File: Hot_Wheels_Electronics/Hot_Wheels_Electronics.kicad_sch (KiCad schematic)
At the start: 21 parts, among them J1 motor_output_a, J2 motor_output_b, J3 Conn_01x05_Socket, M1 motor_driver: DRV8833PW, SW1 main_switch, U1 esp32-wemos-d1-mini, U2 ESP32-WROOM-32, U3 BMI160, U4 QITN BEC

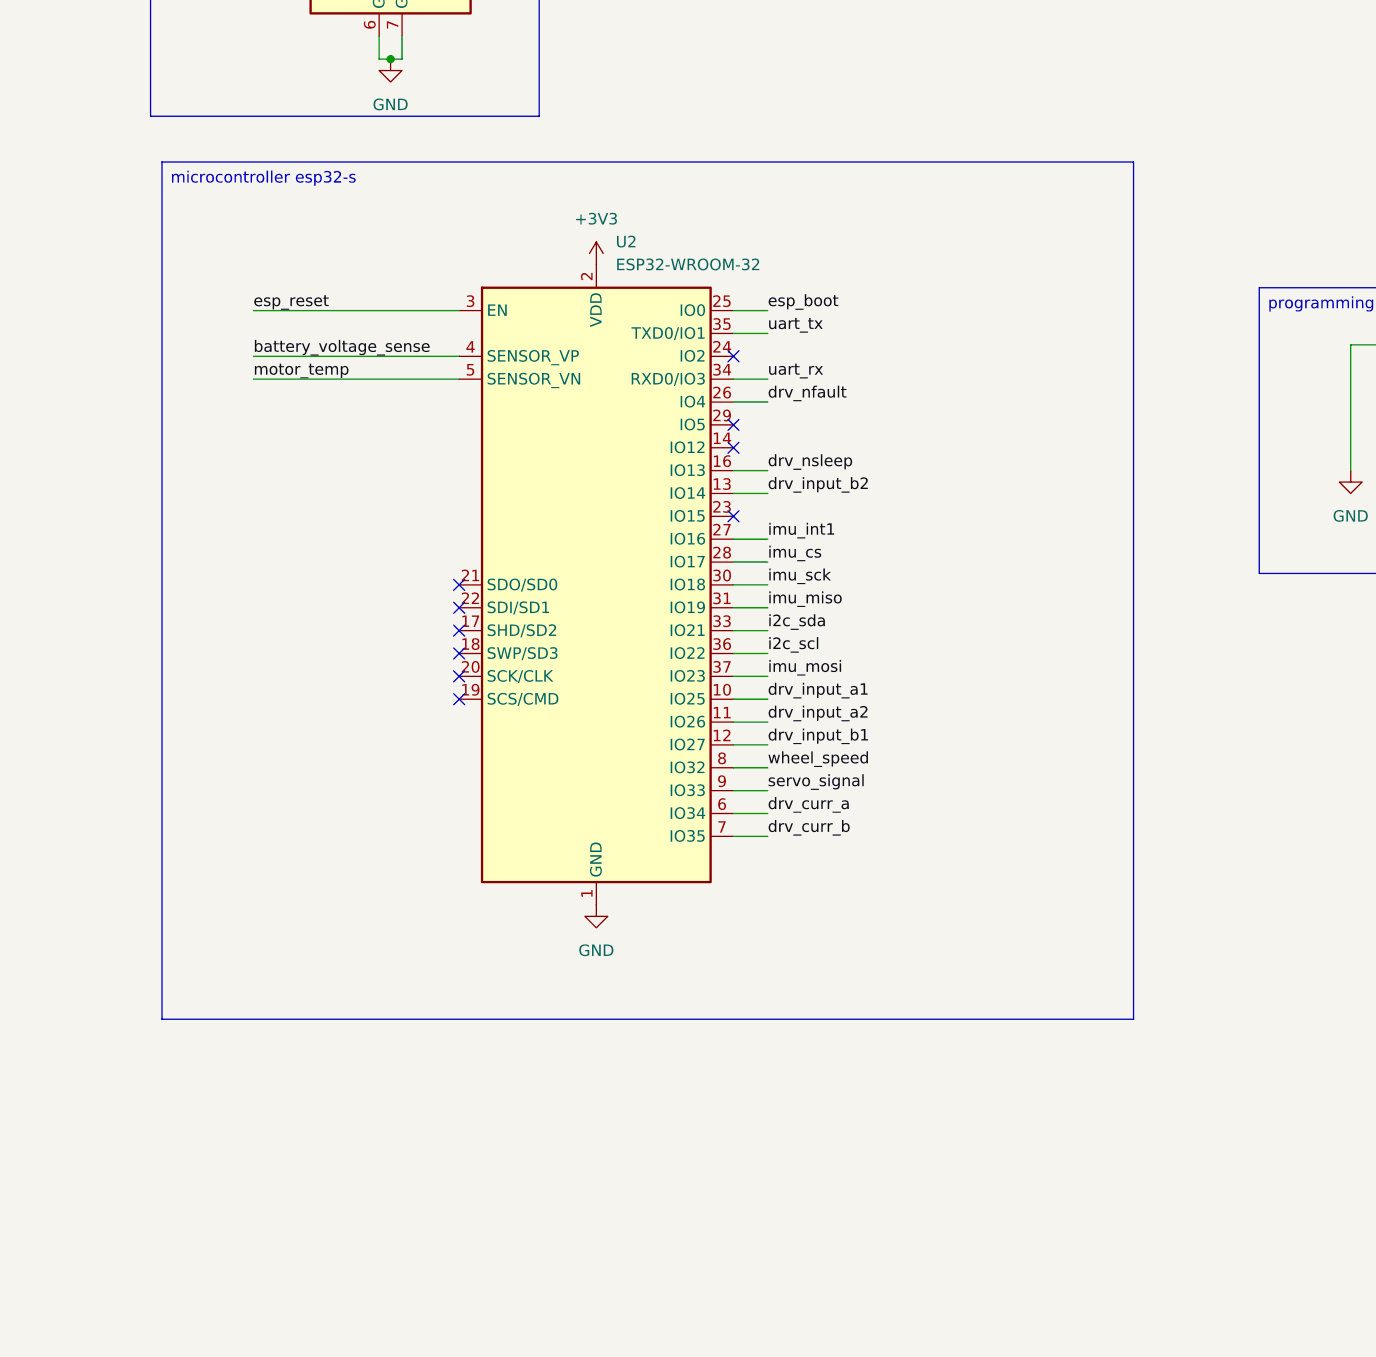
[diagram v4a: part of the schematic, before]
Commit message: add the reset and boot schematic components
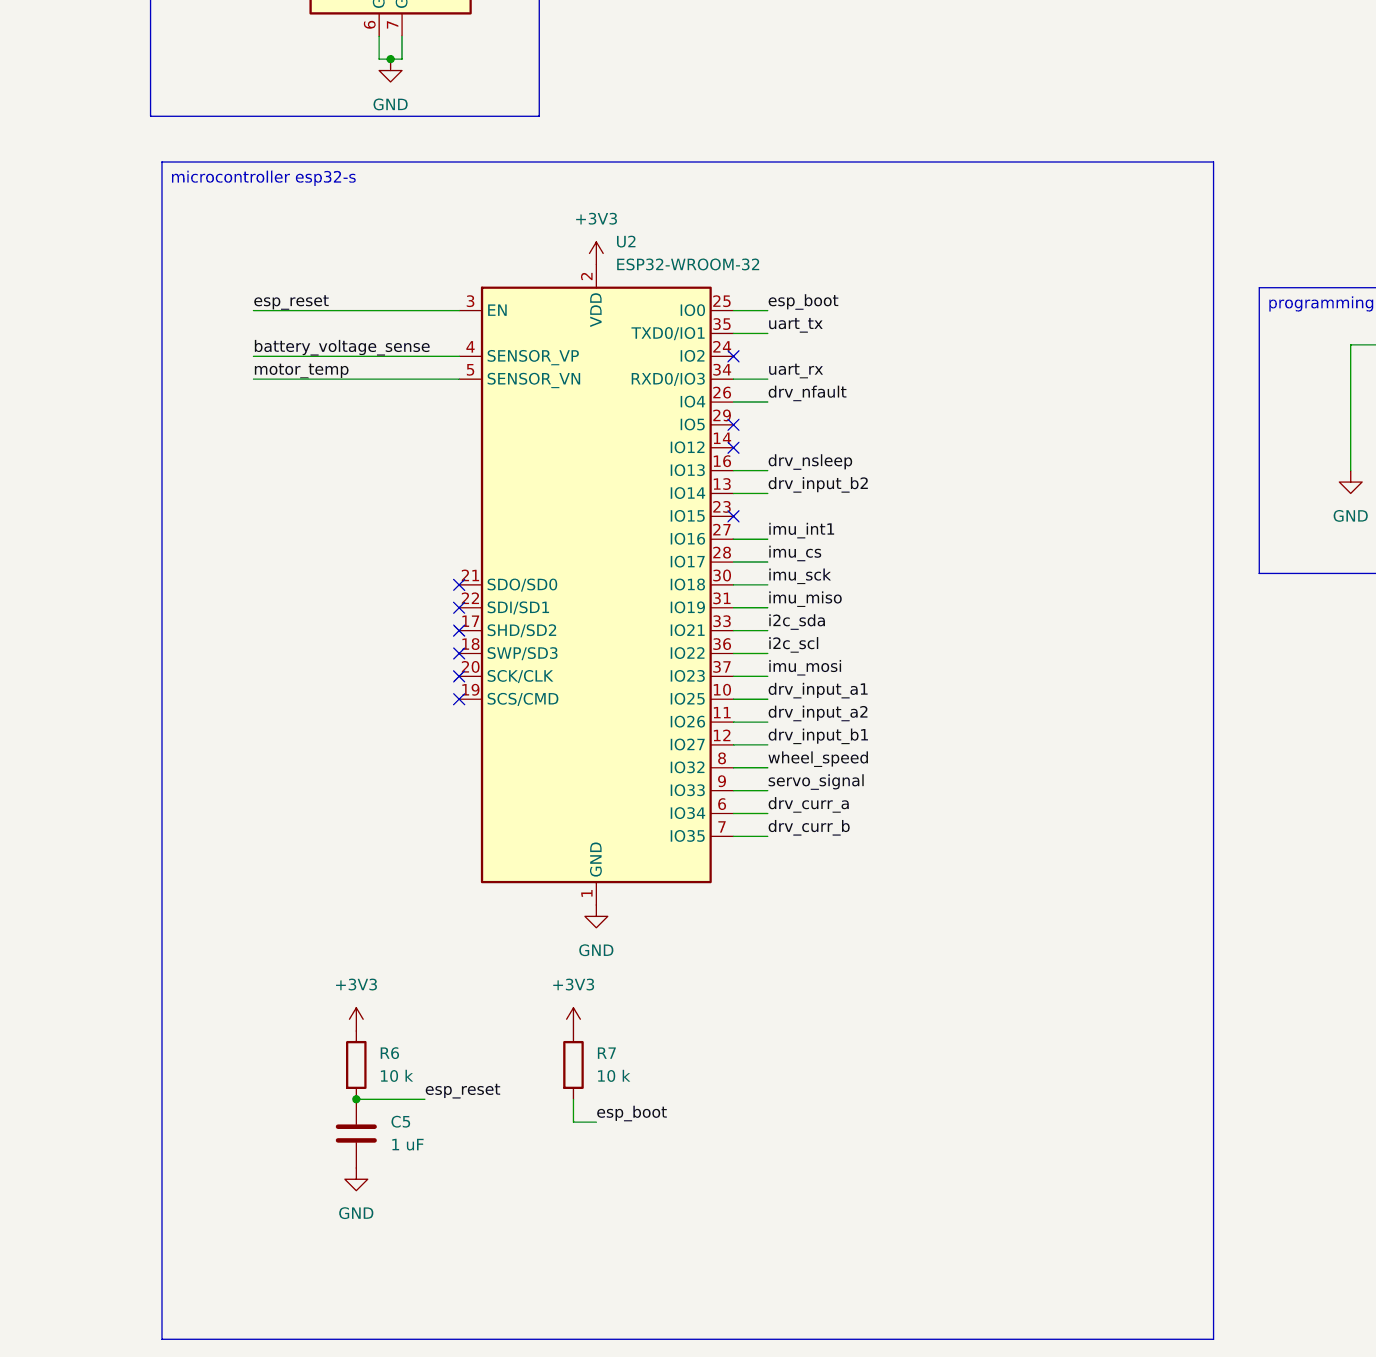
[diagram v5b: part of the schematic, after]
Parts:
- added C5: 1 uF, symbol Device:C
- added R6, R7: 10 k, symbol Device:R
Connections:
- net +3V3: now also R6.1, R7.1
- net GND: now also C5.2
- net esp_boot: now also R7.2
- net esp_reset: now also C5.1, R6.2

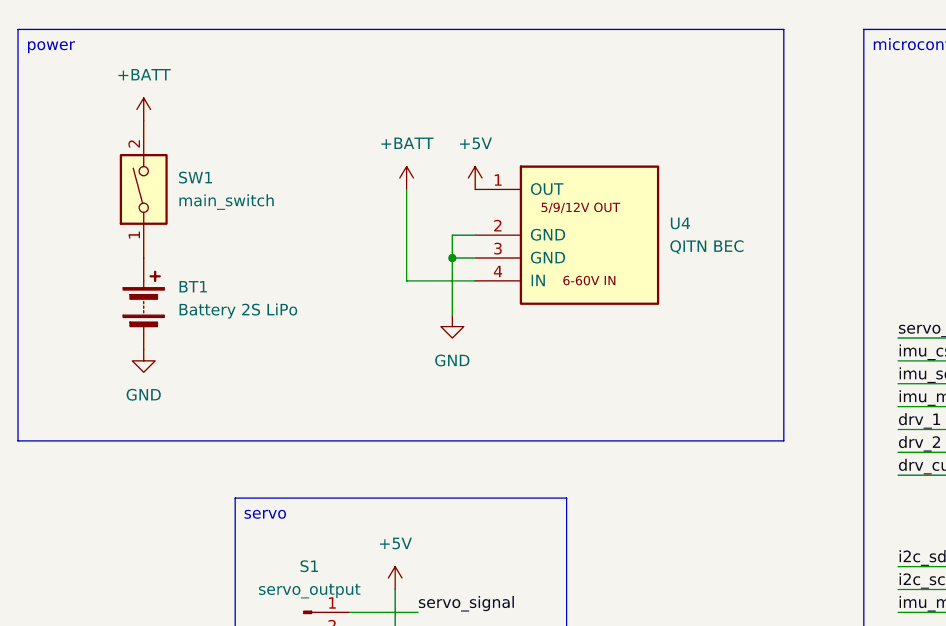
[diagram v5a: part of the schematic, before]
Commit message: added dedicated 3.3V and 6V buck modules
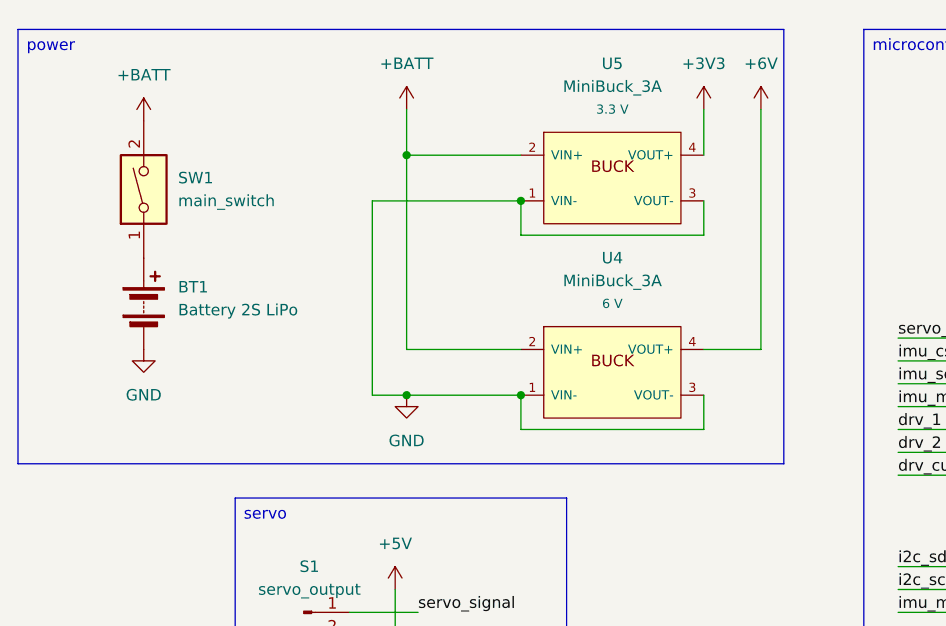
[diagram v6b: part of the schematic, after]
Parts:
- removed U4: QITN BEC, QITN_Matek_Micro_BEC:BEC_QITN_Matek_Micro_18x16mm_Castellated, symbol QITN_Matek_Micro_BEC:QITN_Matek_Micro_BEC_6-60V_5V9V12V
- added U4, U5: MiniBuck_3A, MiniBuck:MiniBuck_CN3903_17.5x12mm, symbol MiniBuck:MiniBuck_3A
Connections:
- net +3V3: now also U5.4 (VOUT+)
- net +BATT: now also U4.2 (VIN+), U5.2 (VIN+)
- net GND: now also U4.1 (VIN-), U4.3 (VOUT-), U5.1 (VIN-), U5.3 (VOUT-)
- new net +6V: U4.4 (VOUT+)

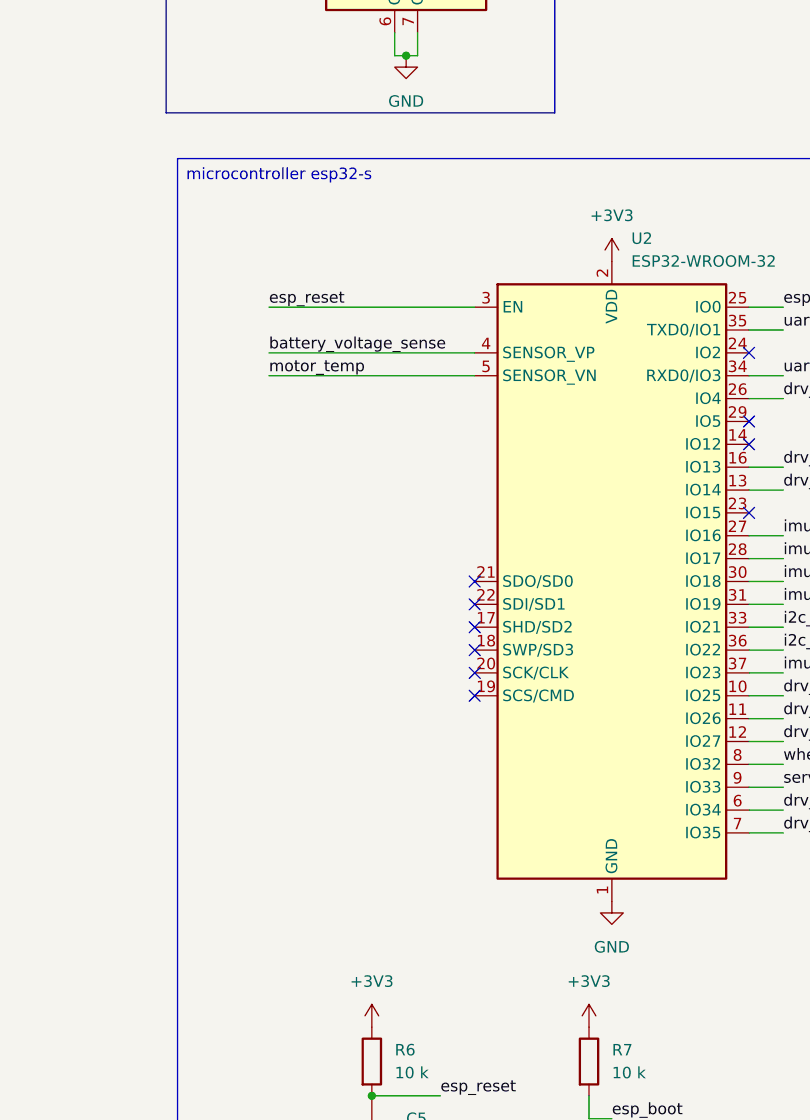
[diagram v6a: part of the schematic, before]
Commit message: renamed to esp32-u
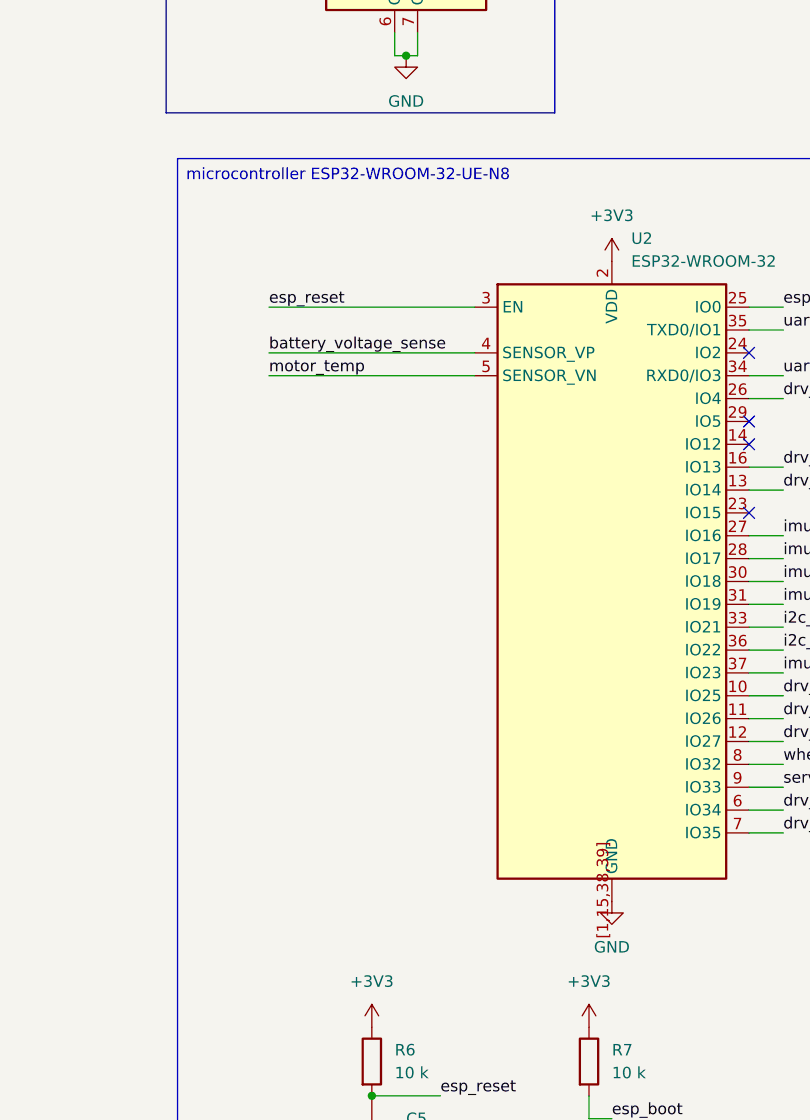
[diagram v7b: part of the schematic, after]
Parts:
- U2: footprint RF_Module:ESP32-WROOM-32 -> RF_Module:ESP32-WROOM-32UE; symbol RF_Module:ESP32-WROOM-32 -> RF_Module:ESP32-WROOM-32UE
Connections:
- net GND: now also U2.[1,15,38,39] (GND); no longer U2.1 (GND), U2.15 (GND), U2.38 (GND), U2.39 (GND)
- no-connect marks 10 -> 4
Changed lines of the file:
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@@
 		)
 	)
-	(text_box "microcontroller esp32-s"
+	(text_box "microcontroller ESP32-WROOM-32-UE-N8"
 		(exclude_from_sim no)
 		(at 204.47 63.5 0)
@@
 	)
 	(no_connect
-		(at 237.49 110.49)
-	)
-	(no_connect
 		(at 267.97 85.09)
-	)
-	(no_connect
-		(at 237.49 113.03)
 	)
 	(no_connect
@@
 	)
 	(no_connect
-		(at 237.49 118.11)
-	)
-	(no_connect
 		(at 267.97 92.71)
-	)
-	(no_connect
-		(at 237.49 120.65)
-	)
-	(no_connect
-		(at 237.49 115.57)
 	)
 	(no_connect
 		(at 267.97 95.25)
-	)
-	(no_connect
-		(at 237.49 123.19)
 	)
 	(wire
@@
 	)
 	(symbol
-		(lib_id "RF_Module:ESP32-WROOM-32")
+		(lib_id "RF_Module:ESP32-WROOM-32UE")
 		(at 252.73 110.49 0)
 		(unit 1)
@@
 			)
 		)
-		(property "Footprint" "RF_Module:ESP32-WROOM-32"
-			(at 252.73 148.59 0)
+		(property "Footprint" "RF_Module:ESP32-WROOM-32UE"
+			(at 269.24 144.78 0)
 			(hide yes)
 			(show_name no)
@@
 			)
 		)
-		(property "Datasheet" "https://www.espressif.com/sites/default/files/documentation/esp32-wroom-32_datasheet_en.pdf"
-			(at 245.11 109.22 0)
-			(hide yes)
-			(show_name no)
-			(do_not_autoplace no)
-			(effects
-				(font
-					(size 1.27 1.27)
-				)
-			)
-		)
-		(property "Description" "RF Module, ESP32-D0WDQ6 SoC, Wi-Fi 802.11b/g/n, Bluetooth, BLE, 32-bit, 2.7-3.6V, onboard antenna, SMD"
+		(property "Datasheet" "https://www.espressif.com/sites/default/files/documentation/esp32-wroom-32e_esp32-wroom-32ue_datasheet_en.pdf"
 			(at 252.73 110.49 0)
 			(hide yes)
@@
 			)
 		)
+		(property "Description" "RF Module, ESP32-D0WD-V3 SoC, without PSRAM, Wi-Fi 802.11b/g/n, Bluetooth, BLE, 32-bit, 2.7-3.6V, external antenna, SMD"
+			(at 252.73 110.49 0)
+			(hide yes)
+			(show_name no)
+			(do_not_autoplace no)
+			(effects
+				(font
+					(size 1.27 1.27)
+				)
+			)
+		)
 		(pin "31"
 		)
 		(pin "34"
 		)
-		(pin "39"
+		(pin "[1,15,38,39]"
 		)
 		(pin "37"
@@
 		(pin "33"
 		)
-		(pin "38"
-		)
 		(pin "27"
 		)
@@
 		(pin "4"
 		)
-		(pin "15"
-		)
 		(pin "16"
 		)
@@
 		(pin "2"
 		)
-		(pin "1"
-		)
 		(pin "14"

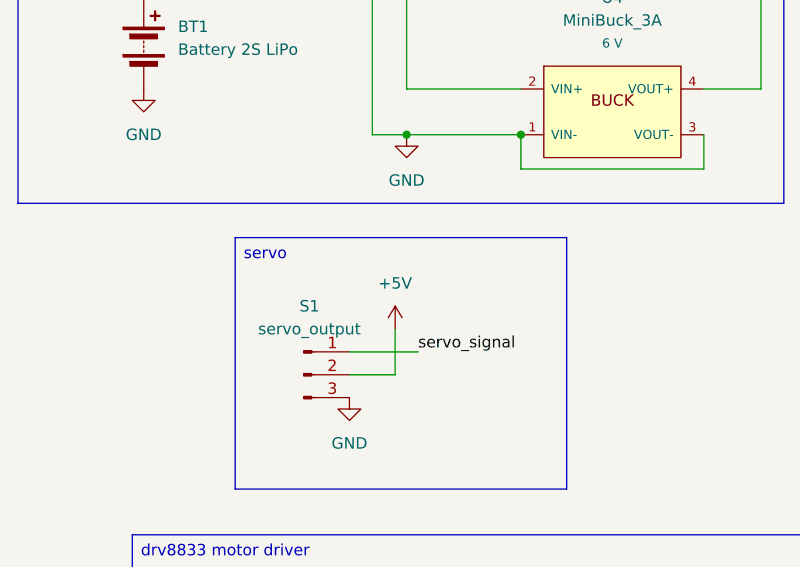
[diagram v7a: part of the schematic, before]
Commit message: fix: servo VIN to +6V
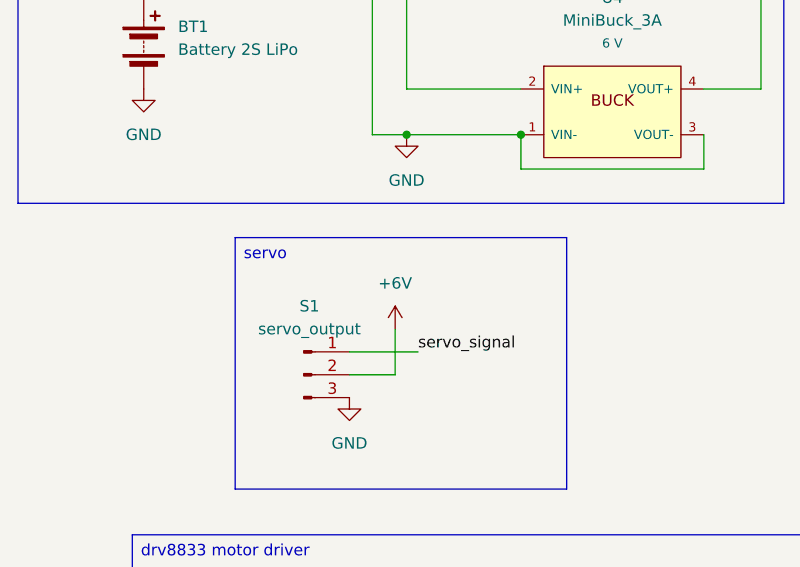
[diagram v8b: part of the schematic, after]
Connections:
- net +5V: no longer S1.2 (Pin_2)
- net +6V: now also S1.2 (Pin_2)
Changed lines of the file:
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@@
-	)
-	(symbol
-		(lib_id "power:+5V")
-		(at 62.23 78.74 0)
-		(unit 1)
-		(body_style 1)
-		(exclude_from_sim no)
-		(in_bom yes)
-		(on_board yes)
-		(in_pos_files yes)
-		(dnp no)
-		(fields_autoplaced yes)
-		(property "Reference" "#PWR09"
-			(at 62.23 82.55 0)
-			(hide yes)
-			(show_name no)
-			(do_not_autoplace no)
-			(effects
-				(font
-					(size 1.27 1.27)
-				)
-			)
-		)
-		(property "Value" "+5V"
-			(at 62.23 73.66 0)
-			(show_name no)
-			(do_not_autoplace no)
-			(effects
-				(font
-					(size 1.27 1.27)
-				)
-			)
-		)
-		(property "Footprint" ""
-			(at 62.23 78.74 0)
-			(hide yes)
-			(show_name no)
-			(do_not_autoplace no)
-			(effects
-				(font
-					(size 1.27 1.27)
-				)
-			)
-		)
-		(property "Datasheet" ""
-			(at 62.23 78.74 0)
-			(hide yes)
-			(show_name no)
-			(do_not_autoplace no)
-			(effects
-				(font
-					(size 1.27 1.27)
-				)
-			)
-		)
-		(property "Description" "Power symbol creates a global label with name \"+5V\""
-			(at 62.23 78.74 0)
-			(hide yes)
-			(show_name no)
-			(do_not_autoplace no)
-			(effects
-				(font
-					(size 1.27 1.27)
-				)
-			)
-		)
-		(pin "1"
-		)
-		(instances
-			(project "Hot_Wheels_Electronics"
-				(path "/753fef37-370a-4893-8adb-358cd7fc1669"
-					(reference "#PWR09")
-					(unit 1)
-				)
-			)
-		)
 	)
 	(symbol
@@
 				(path "/753fef37-370a-4893-8adb-358cd7fc1669"
 					(reference "#PWR03")
+					(unit 1)
+				)
+			)
+		)
+	)
+	(symbol
+		(lib_id "power:+6V")
+		(at 62.23 78.74 0)
+		(unit 1)
+		(body_style 1)
+		(exclude_from_sim no)
+		(in_bom yes)
+		(on_board yes)
+		(in_pos_files yes)
+		(dnp no)
+		(fields_autoplaced yes)
+		(property "Reference" "#PWR09"
+			(at 62.23 82.55 0)
+			(hide yes)
+			(show_name no)
+			(do_not_autoplace no)
+			(effects
+				(font
+					(size 1.27 1.27)
+				)
+			)
+		)
+		(property "Value" "+6V"
+			(at 62.23 73.66 0)
+			(show_name no)
+			(do_not_autoplace no)
+			(effects
+				(font
+					(size 1.27 1.27)
+				)
+			)
+		)
+		(property "Footprint" ""
+			(at 62.23 78.74 0)
+			(hide yes)
+			(show_name no)
+			(do_not_autoplace no)
+			(effects
+				(font
+					(size 1.27 1.27)
+				)
+			)
+		)
+		(property "Datasheet" ""
+			(at 62.23 78.74 0)
+			(hide yes)
+			(show_name no)
+			(do_not_autoplace no)
+			(effects
+				(font
+					(size 1.27 1.27)
+				)
+			)
+		)
+		(property "Description" "Power symbol creates a global label with name \"+6V\""
+			(at 62.23 78.74 0)
+			(hide yes)
+			(show_name no)
+			(do_not_autoplace no)
+			(effects
+				(font
+					(size 1.27 1.27)
+				)
+			)
+		)
+		(pin "1"
+		)
+		(instances
+			(project "Hot_Wheels_Electronics"
+				(path "/753fef37-370a-4893-8adb-358cd7fc1669"
+					(reference "#PWR09")
 					(unit 1)
 				)
@@
 		(members "02e6cbf2-d642-4879-af54-b22362d7b191" "07f69d92-3cd5-4135-9105-22ac4b3c81ec"
 			"17040d0f-3602-4ff4-81a5-da3a45db6dbc" "85777476-fab3-4af8-8309-0fb6b166dc6a"
-			"99fb0b4b-4091-4ce1-a384-65eb5d0ffee9" "9f39db7f-b2ed-4d29-9364-21f243226ff3"
-			"b6706b2a-33e2-43b6-8358-153c1c58b17a" "e8528510-df4f-40b0-b7c8-9f66a5899095"
-		)
-	)
+			"9f39db7f-b2ed-4d29-9364-21f243226ff3" "b6706b2a-33e2-43b6-8358-153c1c58b17a"
+			"e8528510-df4f-40b0-b7c8-9f66a5899095"
+		)
+	)
